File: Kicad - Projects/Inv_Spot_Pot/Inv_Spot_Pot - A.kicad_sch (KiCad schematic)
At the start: 70 parts, among them J1 Screw_Terminal_01x03, J2 PWM, J3 Display_Power, J4 24V, Q1 60N60, Q2 60N60, Q3 60N60, Q4 60N60, T1 Transformer_1P_2S

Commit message: Exploração da Placa de Potência
Explorando diferentes posições para os componentes da placa de potência
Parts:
- removed U3: (no value), Custom_Transformer:EEL25V 6T+6T, symbol Custom_Transformers:EEL25V_6T+6T
- renumbered D5 to D10, D10 to D11, D11 to D12, D12 to D13, D13 to D14, D14 to D15, D15 to D16, D16 to D17, D17 to D18, D3 to D9
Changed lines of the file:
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@@
 		(in_pos_files yes)
 		(dnp no)
-		(property "Reference" "D15"
+		(property "Reference" "D16"
 			(at 258.826 118.364 0)
 			(show_name no)
@@
 			(project "Inv_Spot_Pot - A"
 				(path "/e27abe51-96c0-4fdf-ba00-b5a281cd0e9c"
-					(reference "D15")
+					(reference "D16")
 					(unit 1)
 				)
@@
 		(in_pos_files yes)
 		(dnp no)
-		(property "Reference" "D10"
+		(property "Reference" "D11"
 			(at 259.334 50.038 0)
 			(show_name no)
@@
 			(project "Inv_Spot_Pot - A"
 				(path "/e27abe51-96c0-4fdf-ba00-b5a281cd0e9c"
-					(reference "D10")
+					(reference "D11")
 					(unit 1)
 				)
@@
 		(in_pos_files yes)
 		(dnp no)
-		(property "Reference" "D14"
+		(property "Reference" "D15"
 			(at 259.08 108.712 0)
 			(show_name no)
@@
 			(project "Inv_Spot_Pot - A"
 				(path "/e27abe51-96c0-4fdf-ba00-b5a281cd0e9c"
-					(reference "D14")
+					(reference "D15")
 					(unit 1)
 				)
@@
 		(in_pos_files yes)
 		(dnp no)
-		(property "Reference" "D17"
+		(property "Reference" "D18"
 			(at 258.826 136.144 0)
 			(show_name no)
@@
 			(project "Inv_Spot_Pot - A"
 				(path "/e27abe51-96c0-4fdf-ba00-b5a281cd0e9c"
-					(reference "D17")
+					(reference "D18")
 					(unit 1)
 				)
@@
 		(in_pos_files yes)
 		(dnp no)
-		(property "Reference" "D12"
+		(property "Reference" "D13"
 			(at 258.826 69.342 0)
 			(show_name no)
@@
 			(project "Inv_Spot_Pot - A"
 				(path "/e27abe51-96c0-4fdf-ba00-b5a281cd0e9c"
-					(reference "D12")
+					(reference "D13")
 					(unit 1)
 				)
@@
 		(in_pos_files yes)
 		(dnp no)
-		(property "Reference" "D13"
+		(property "Reference" "D14"
 			(at 259.588 83.312 0)
 			(show_name no)
@@
 			(project "Inv_Spot_Pot - A"
 				(path "/e27abe51-96c0-4fdf-ba00-b5a281cd0e9c"
-					(reference "D13")
+					(reference "D14")
 					(unit 1)
 				)
@@
 		(in_pos_files yes)
 		(dnp no)
-		(property "Reference" "D3"
+		(property "Reference" "D9"
 			(at 164.7825 147.32 0)
 			(show_name no)
@@
 			(project "Inv_Spot_Pot - A"
 				(path "/e27abe51-96c0-4fdf-ba00-b5a281cd0e9c"
-					(reference "D3")
+					(reference "D9")
 					(unit 1)
 				)
@@
 		(in_pos_files yes)
 		(dnp no)
-		(property "Reference" "D11"
+		(property "Reference" "D12"
 			(at 259.08 59.182 0)
 			(show_name no)
@@
 			(project "Inv_Spot_Pot - A"
 				(path "/e27abe51-96c0-4fdf-ba00-b5a281cd0e9c"
-					(reference "D11")
+					(reference "D12")
 					(unit 1)
 				)
@@
 	)
 	(symbol
-		(lib_id "Custom_Transformers:EEL25V_6T+6T")
-		(at 177.8 58.42 0)
-		(unit 1)
-		(body_style 1)
-		(exclude_from_sim no)
-		(in_bom yes)
-		(on_board yes)
-		(in_pos_files yes)
-		(dnp no)
-		(fields_autoplaced yes)
-		(property "Reference" "U3"
-			(at 177.8 58.42 0)
-			(show_name no)
-			(do_not_autoplace no)
-			(effects
-				(font
-					(size 1.27 1.27)
-				)
-			)
-		)
-		(property "Value" ""
-			(at 177.8 58.42 0)
-			(show_name no)
-			(do_not_autoplace no)
-			(effects
-				(font
-					(size 1.27 1.27)
-				)
-			)
-		)
-		(property "Footprint" "Custom_Transformer:EEL25V 6T+6T"
-			(at 177.8 58.42 0)
-			(hide yes)
-			(show_name no)
-			(do_not_autoplace no)
-			(effects
-				(font
-					(size 1.27 1.27)
-				)
-			)
-		)
-		(property "Datasheet" ""
-			(at 177.8 58.42 0)
-			(hide yes)
-			(show_name no)
-			(do_not_autoplace no)
-			(effects
-				(font
-					(size 1.27 1.27)
-				)
-			)
-		)
-		(property "Description" ""
-			(at 177.8 58.42 0)
-			(hide yes)
-			(show_name no)
-			(do_not_autoplace no)
-			(effects
-				(font
-					(size 1.27 1.27)
-				)
-			)
-		)
-		(pin "3"
-		)
-		(pin "9"
-		)
-		(pin "2"
-		)
-		(pin "5"
-		)
-		(pin "12"
-		)
-		(pin "11"
-		)
-		(pin "1"
-		)
-		(pin "6"
-		)
-		(pin "7"
-		)
-		(pin "8"
-		)
-		(pin "4"
-		)
-		(pin "10"
-		)
-		(instances
-			(project "Inv_Spot_Pot - A"
-				(path "/e27abe51-96c0-4fdf-ba00-b5a281cd0e9c"
-					(reference "U3")
-					(unit 1)
-				)
-			)
-		)
-	)
-	(symbol
 		(lib_id "power:VCC")
 		(at 93.98 177.8 0)
@@
 		(in_pos_files yes)
 		(dnp no)
-		(property "Reference" "D5"
+		(property "Reference" "D10"
 			(at 164.7825 121.92 0)
 			(show_name no)
@@
 			(project "Inv_Spot_Pot - A"
 				(path "/e27abe51-96c0-4fdf-ba00-b5a281cd0e9c"
-					(reference "D5")
+					(reference "D10")
 					(unit 1)
 				)
@@
 		(in_pos_files yes)
 		(dnp no)
-		(property "Reference" "D16"
+		(property "Reference" "D17"
 			(at 258.826 127.254 0)
 			(show_name no)
@@
 			(project "Inv_Spot_Pot - A"
 				(path "/e27abe51-96c0-4fdf-ba00-b5a281cd0e9c"
-					(reference "D16")
+					(reference "D17")
 					(unit 1)
 				)

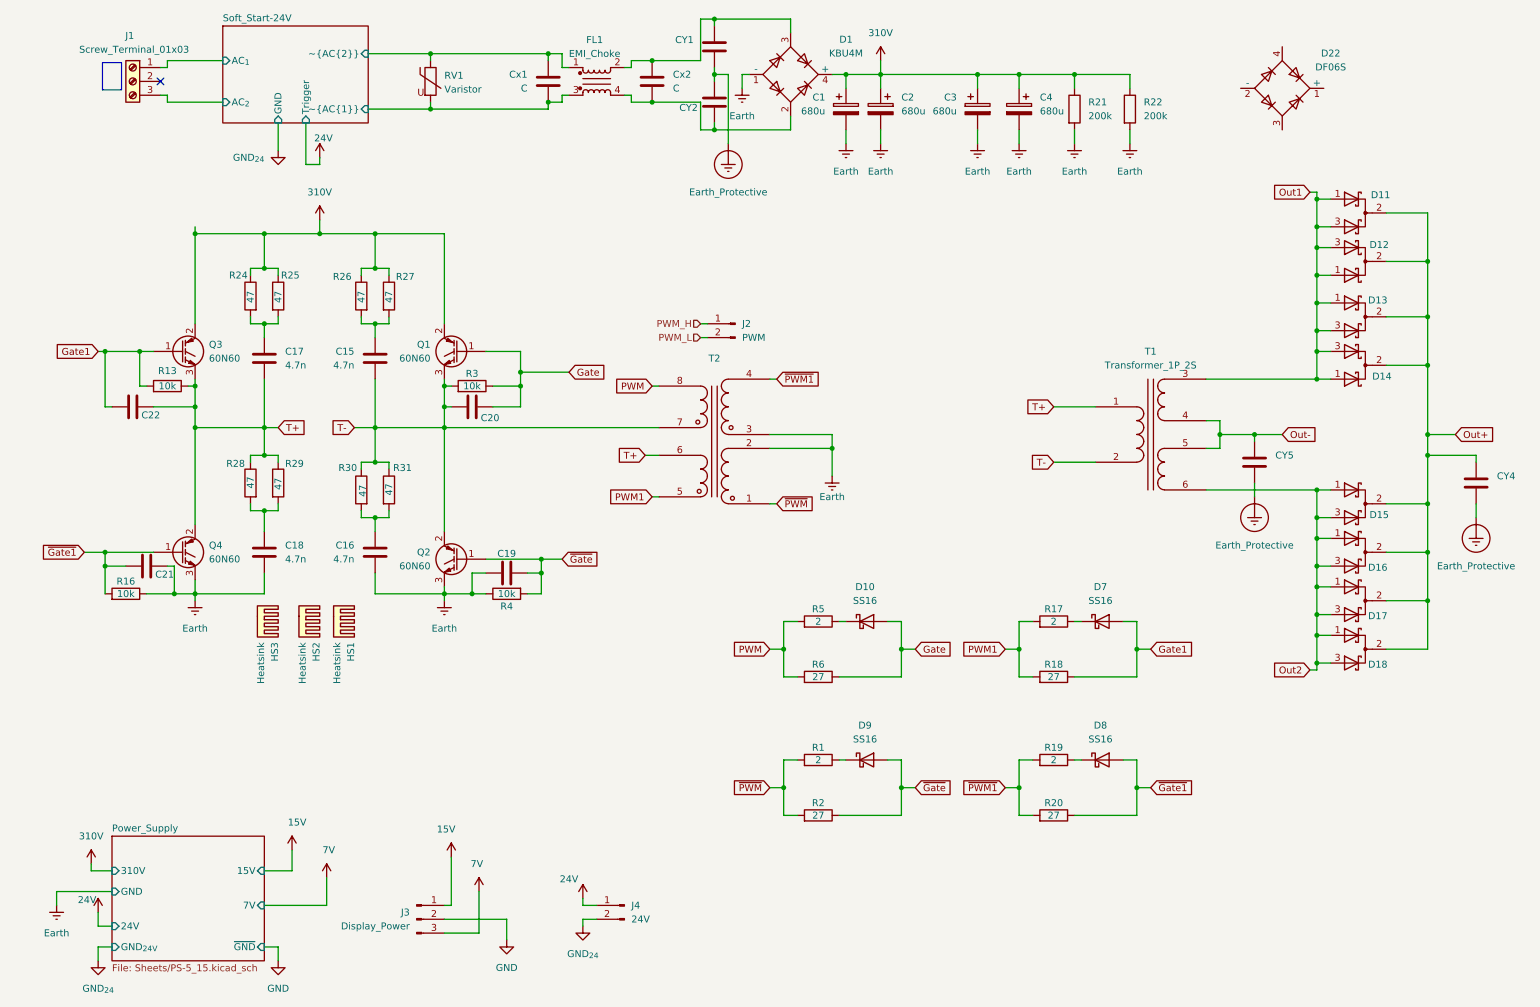
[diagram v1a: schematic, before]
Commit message: Adicionada Fuaração
Adicionada furação de montagem na placa de display, 4 furos M3 nos cantos da placa
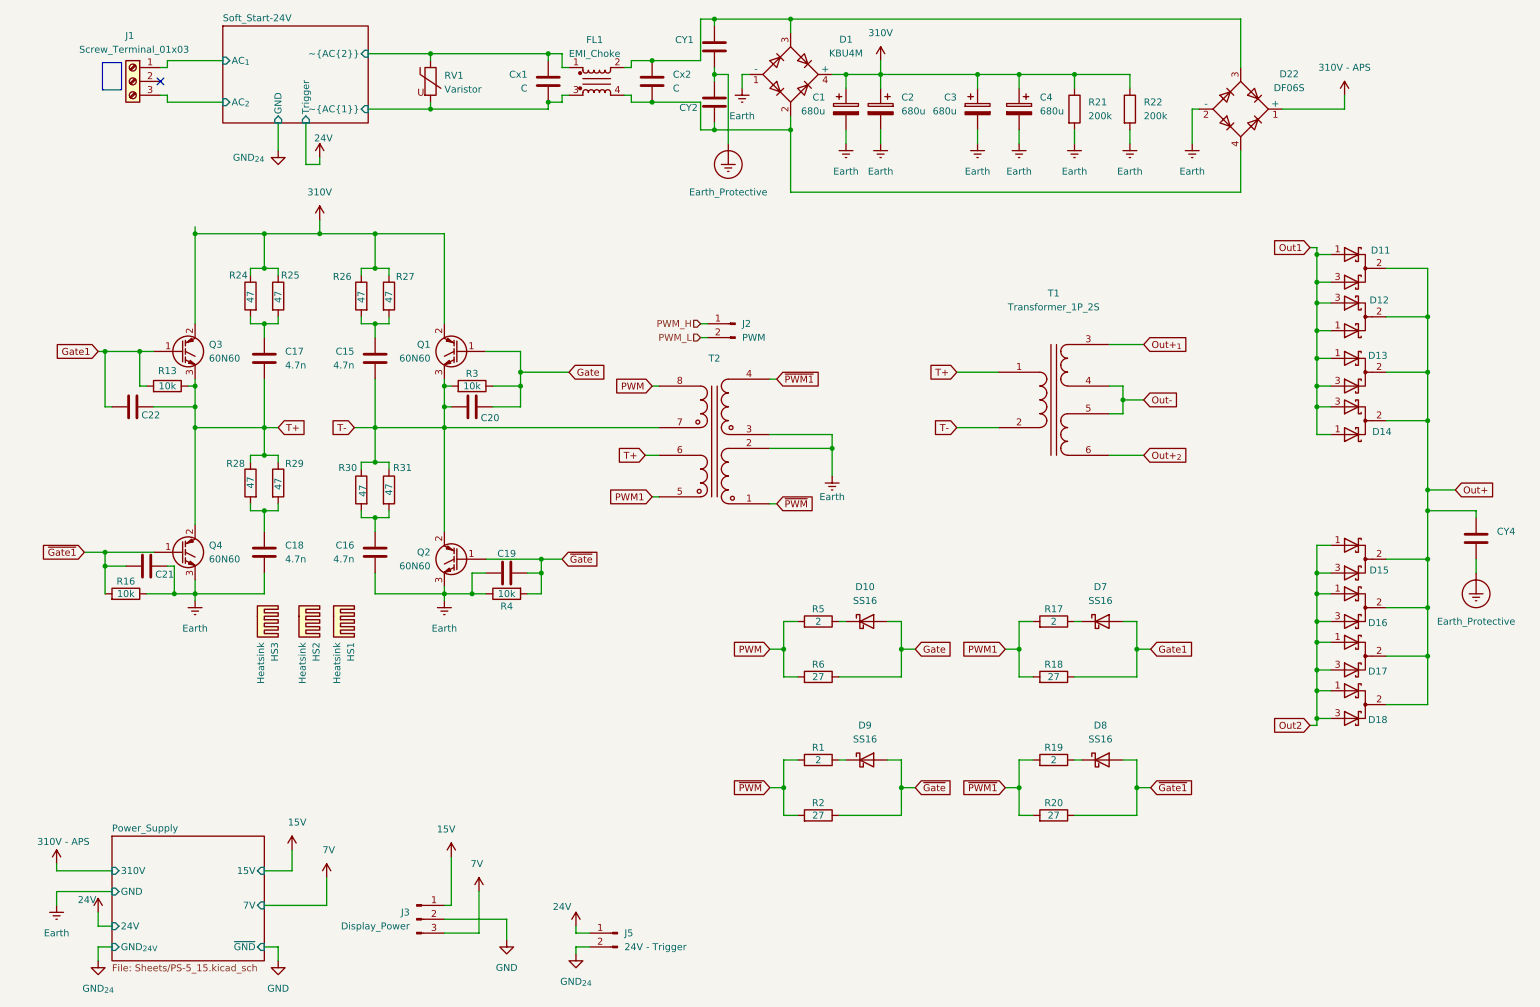
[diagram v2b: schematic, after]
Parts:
- removed CY5: C, Capacitor_THT:C_Disc_D7.0mm_W2.5mm_P5.00mm, symbol Device:C
- removed J4: 24V, Connector_JST:JST_XH_B2B-XH-A_1x02_P2.50mm_Vertical, symbol Connector:Conn_01x02_Pin
- added J5: 24V - Trigger, Connector_PinHeader_2.54mm:PinHeader_1x02_P2.54mm_Vertical, symbol Connector:Conn_01x02_Pin
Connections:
- net 24V: now also J5.1 (Pin_1)
- net Earth: now also D22.2 (-)
- net GND_{24}: now also J5.2 (Pin_2)
- net Out1: no longer T1.3 (SA)
- net Out2: no longer T1.6 (SD)
- net at CY2.2, Cx2.2, D1.2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: now also D22.4
- net at CY1.1, Cx2.1, D1.3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: now also D22.3
- net 310V - APS: now reaches D22.1 (+)
- new net Out+_{1}: T1.3 (SA)
- new net Out+_{2}: T1.6 (SD)
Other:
- moved on the sheet: CY4, D11, D12, D13, D14, D15, D16, D17, D18, D22, T1

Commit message: Finalização da Nova Placa de Potência
Dissipadores reorientados e reposicionados para melhor fluxo de ar

Ajuste dos footprints para dissipadores

Adição de resistores na placa de display para melhor proteção do STM32 e redução do brilho da LCD
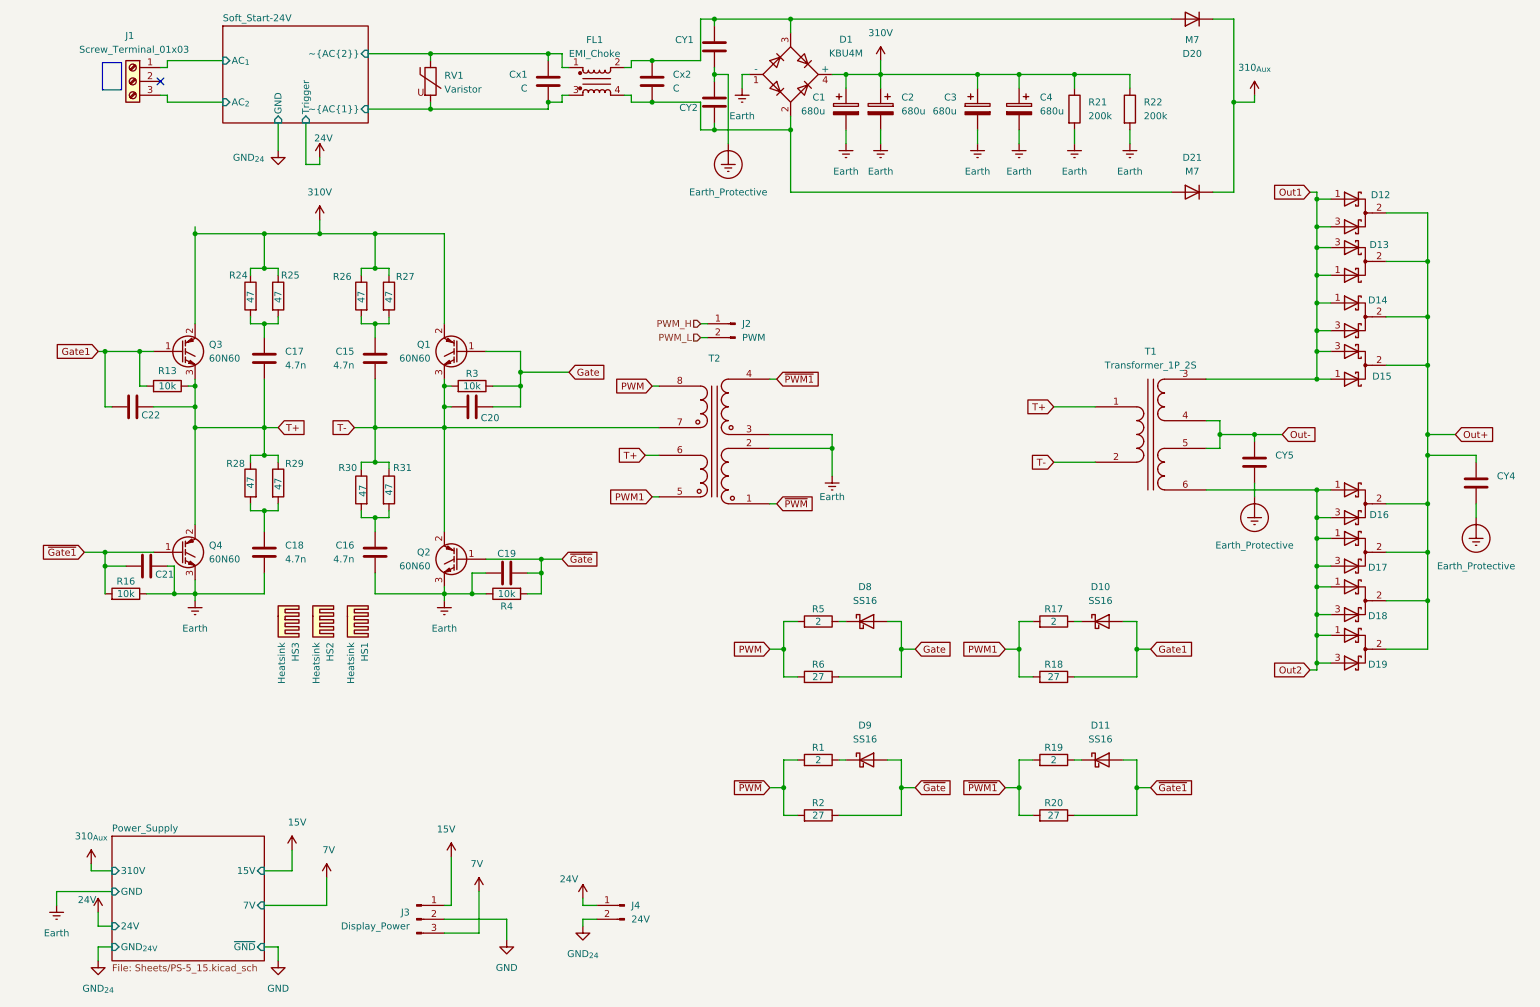
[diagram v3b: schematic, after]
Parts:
- removed D22: DF06S, Diode_SMD:Diode_Bridge_OnSemi_SDIP-4L, symbol Diode_Bridge:DF06S
- removed J5: 24V - Trigger, Connector_PinHeader_2.54mm:PinHeader_1x02_P2.54mm_Vertical, symbol Connector:Conn_01x02_Pin
- added CY5: C, Capacitor_THT:C_Disc_D7.0mm_W2.5mm_P5.00mm, symbol Device:C
- added D20, D21: M7, Diode_SMD:D_SMA, symbol Device:D
- added J4: 24V, Connector_PinHeader_2.54mm:PinHeader_1x02_P2.54mm_Vertical, symbol Connector:Conn_01x02_Pin
- renumbered D7 to D10, D8 to D11, D11 to D12, D12 to D13, D13 to D14, D14 to D15, D15 to D16, D16 to D17, D17 to D18, D18 to D19, D10 to D8
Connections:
- net Out+_{1} is gone; now on net Out1: T1.3 (SA)
- net Out+_{2} is gone; now on net Out2: T1.6 (SD)
- net 24V: now also J4.1 (Pin_1)
- net Earth_Protective: now also CY5.2
- net GND_{24}: now also J4.2 (Pin_2)
- net Out-: now also CY5.1
- net at CY2.2, Cx2.2, D1.2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: now also D21.2 (A)
- net at CY1.1, Cx2.1, D1.3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: now also D20.2 (A)
- new net 310_{Aux}: D20.1 (K), D21.1 (K)
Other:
- moved on the sheet: CY4, D12, D13, D14, D15, D16, D17, D18, D19, HS1, HS2, HS3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
